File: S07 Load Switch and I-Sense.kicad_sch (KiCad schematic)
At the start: 62 parts, among them Q20 BSS138, Q21 BSS138, Q22 BSS138, U10 TLV9002IDSG, U6 TPS22811, U7 TPS22811, U8 TLV9002IDSG, U9 TPS22811

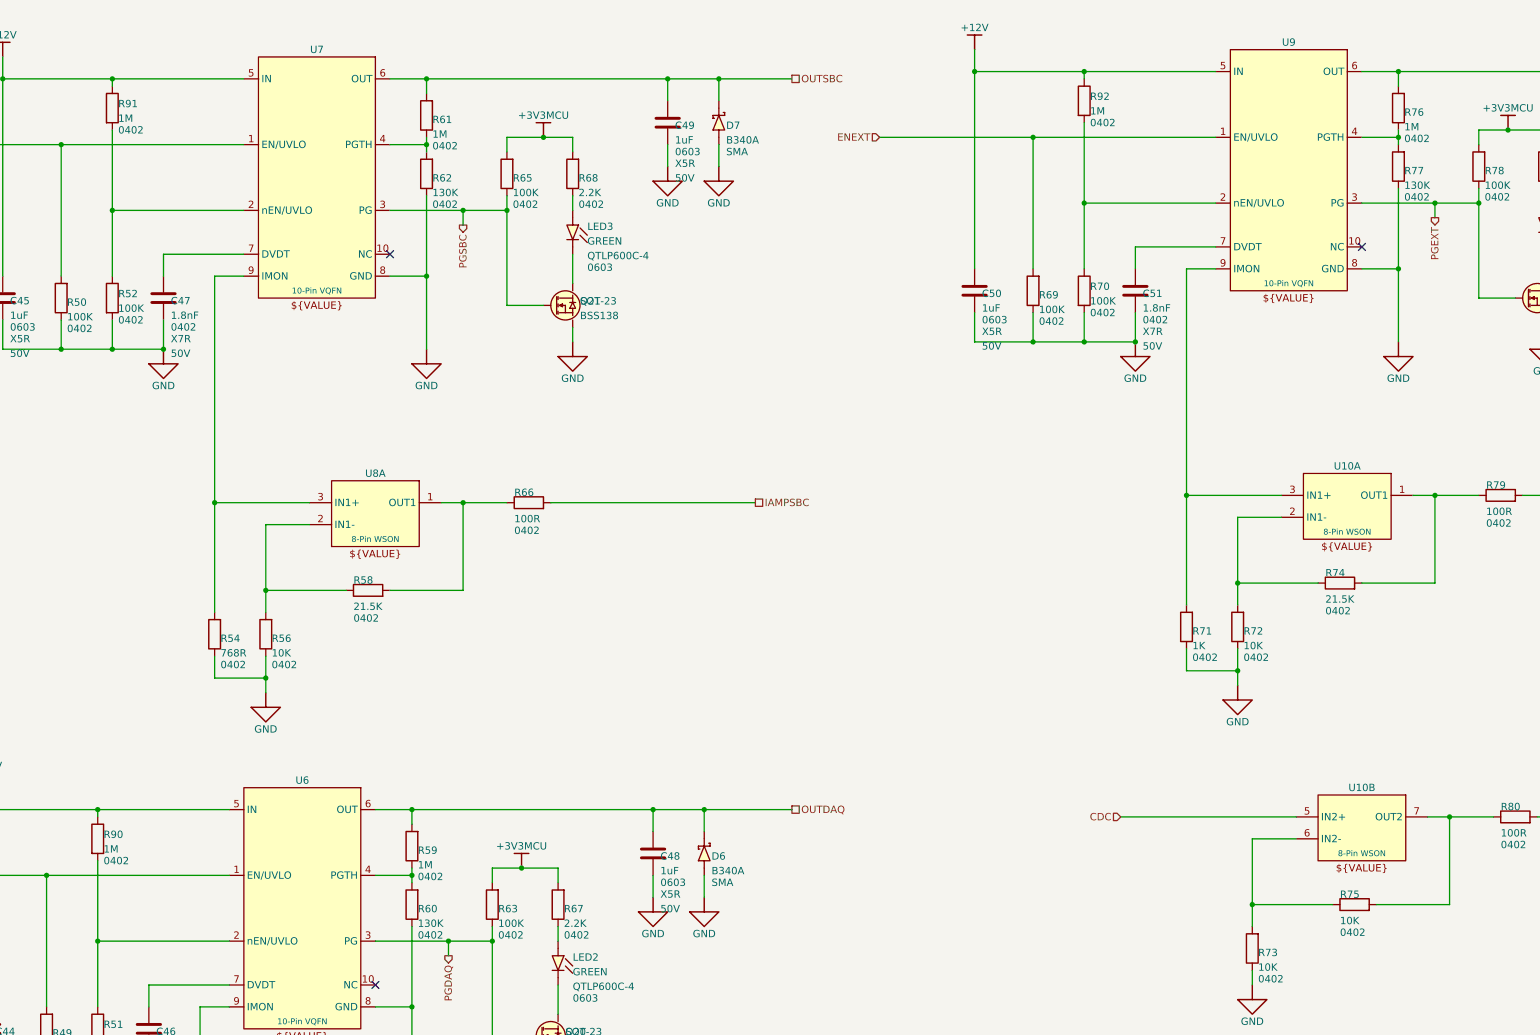
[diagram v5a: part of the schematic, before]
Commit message: Retune load-switch OVLO and PG dividers; add design constraint notes
- R90-R92 1M -> 1.07M: OVLO trips at 14.0 V (13.40-14.69 V) and recovers
  below 12.75 V (at least 12.23 V), so a tripped switch always comes back
  on the 12.03 V rail. R101 (Q23 gate divider) -> 1.07M to share the line.
- PGTH dividers R59/R61/R76 1M -> 100K and R60/R62/R77 130K -> 13K: same
  10.43 V threshold, but the +-1 uA pin leakage now moves it 0.1 V, not
  1 V; worst-case rising 10.93 V instead of 11.84 V.
- Schematic notes for the W16 constraints: J2 contacts (S01), R16 latching
  breaker and ED29/QE29 trip currents (S03), R19 vs L1 saturation (S04),
  R22 presence pull-up (S05), R42 and the U5 MODE/ILIMCOMP/VCC2 pins (S06),
  and the OVLO/PG divider settings (S07).
- README: OVLO and PG divider figures, and the EN_CONST_TDEAD default for
  the I2C build.

Co-Authored-By: Claude Opus 5.5 <noreply@anthropic.com>
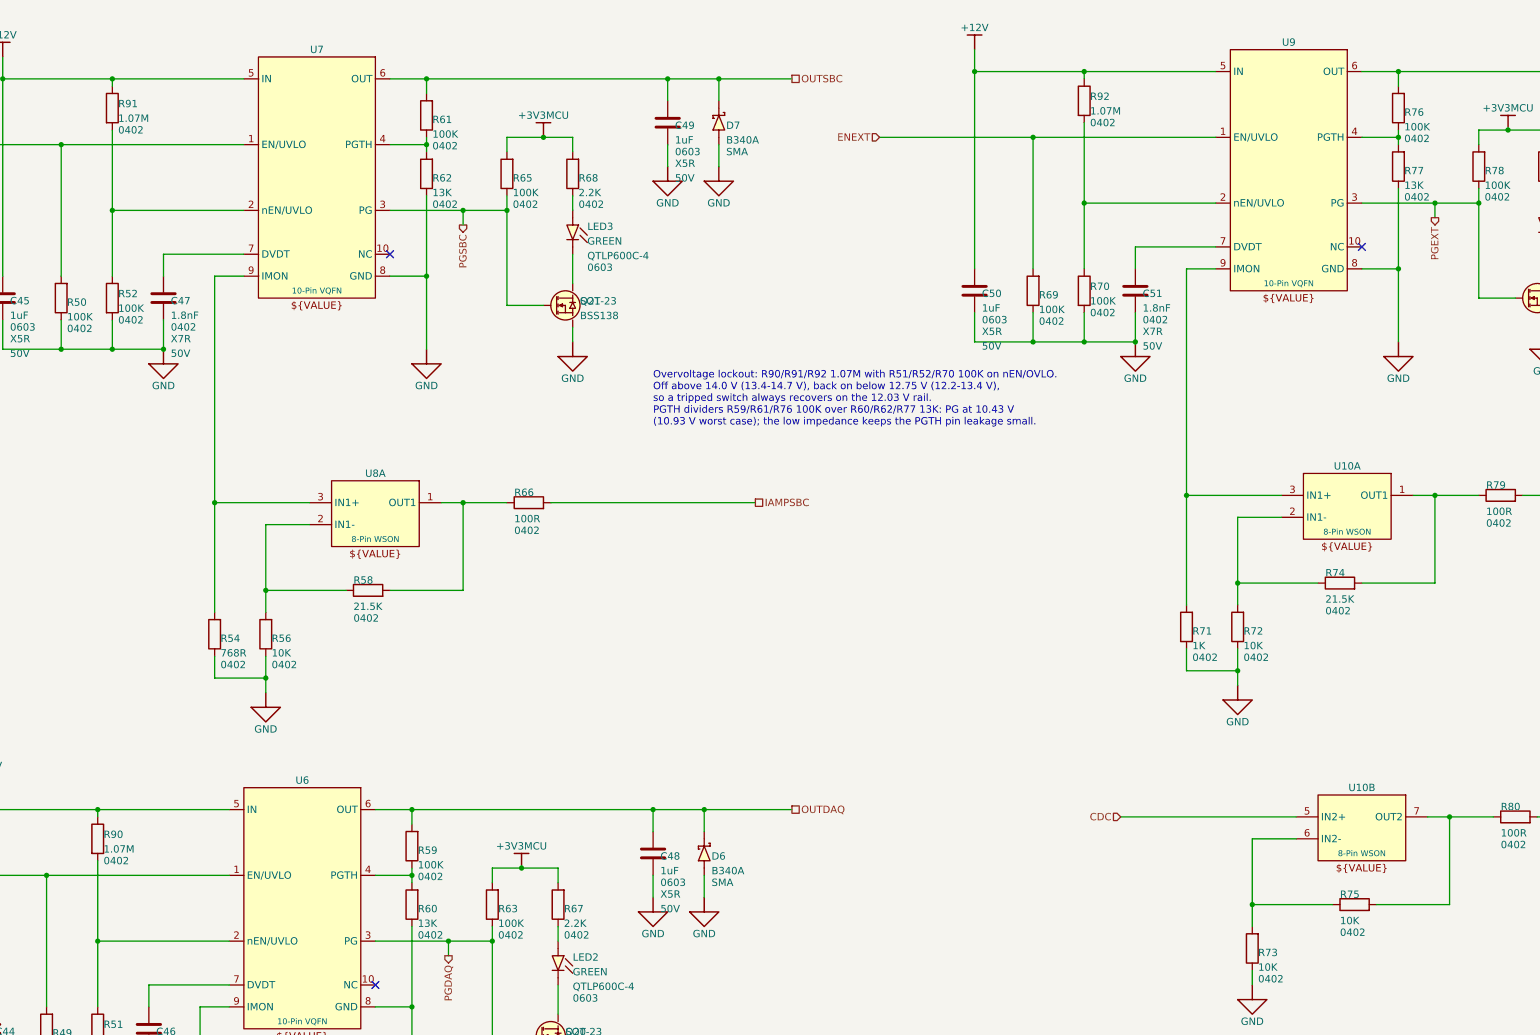
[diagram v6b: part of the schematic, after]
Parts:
- R59, R61, R76: value 1M -> 100K; ALTIUM_VALUE 1M -> 100K
- R60, R62, R77: value 130K -> 13K; ALTIUM_VALUE 130K -> 13K
- R90, R91, R92: value 1M -> 1.07M; ALTIUM_VALUE 1M -> 1.07M
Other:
- note added: "Overvoltage lockout: R90/R91/R92 1.07M with R51/R52/R70 100K on nEN/OVLO. Off above 14.0 V (13.4-14.7 V), back on below 12.75 V (12.2-13.4 V), so a tripped switch always recovers on the 12.03 V rail. PGTH dividers R59/R61/R76 100K over R60/R62/R77 13K: PG at 10.43 V (10.93 V worst case); the low impedance keeps the PGTH pin leakage small."
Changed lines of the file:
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@@
 	(generator_version "10.0")
 	(paper "A3")
+	(text "Overvoltage lockout: R90/R91/R92 1.07M with R51/R52/R70 100K on nEN/OVLO.\nOff above 14.0 V (13.4-14.7 V), back on below 12.75 V (12.2-13.4 V),\nso a tripped switch always recovers on the 12.03 V rail.\nPGTH dividers R59/R61/R76 100K over R60/R62/R77 13K: PG at 10.43 V\n(10.93 V worst case); the low impedance keeps the PGTH pin leakage small."
+		(exclude_from_sim no)
+		(at 170.18 97.79 0)
+		(effects
+			(font
+				(size 1.27 1.27)
+			)
+			(justify left top)
+		)
+	)
 	(text "5"
 		(exclude_from_sim no)
@@
 			)
 		)
-		(property "Value" "1M"
+		(property "Value" "1.07M"
 			(at 77.216 54.61 0)
 			(show_name no)
@@
 			)
 		)
-		(property "Description" "Resistor 1M 1% 0402"
+		(property "Description" "Resistor 1.07M 1% 0402"
 			(at 76.2 52.07 90)
 			(hide yes)
@@
 			)
 		)
-		(property "ALTIUM_VALUE" "1M"
+		(property "ALTIUM_VALUE" "1.07M"
 			(at 75.184 47.752 0)
 			(hide yes)
@@
 			)
 		)
-		(property "Value" "1M"
+		(property "Value" "100K"
 			(at 131.826 55.88 0)
 			(show_name no)
@@
 			)
 		)
-		(property "Description" "Resistor 1M 1% 0402"
+		(property "Description" "Resistor 100K 1% 0402"
 			(at 130.81 53.34 90)
 			(hide yes)
@@
 			)
 		)
-		(property "ALTIUM_VALUE" "1M"
+		(property "ALTIUM_VALUE" "100K"
 			(at 129.794 49.022 0)
 			(hide yes)
@@
 			)
 		)
-		(property "Value" "130K"
+		(property "Value" "13K"
 			(at 300.736 64.77 0)
 			(show_name no)
@@
 			)
 		)
-		(property "Description" "Resistor 130K 1% 0402"
+		(property "Description" "Resistor 13K 1% 0402"
 			(at 299.72 62.23 90)
 			(hide yes)
@@
 			)
 		)
-		(property "ALTIUM_VALUE" "130K"
+		(property "ALTIUM_VALUE" "13K"
 			(at 298.704 57.912 0)
 			(hide yes)
@@
 			)
 		)
-		(property "Value" "1M"
+		(property "Value" "1.07M"
 			(at 246.126 53.34 0)
 			(show_name no)
@@
 			)
 		)
-		(property "Description" "Resistor 1M 1% 0402"
+		(property "Description" "Resistor 1.07M 1% 0402"
 			(at 245.11 50.8 90)
 			(hide yes)
@@
 			)
 		)
-		(property "ALTIUM_VALUE" "1M"
+		(property "ALTIUM_VALUE" "1.07M"
 			(at 244.094 46.482 0)
 			(hide yes)
@@
 			)
 		)
-		(property "Value" "1M"
+		(property "Value" "100K"
 			(at 129.286 182.88 0)
 			(show_name no)
@@
 			)
 		)
-		(property "Description" "Resistor 1M 1% 0402"
+		(property "Description" "Resistor 100K 1% 0402"
 			(at 128.27 180.34 90)
 			(hide yes)
@@
 			)
 		)
-		(property "ALTIUM_VALUE" "1M"
+		(property "ALTIUM_VALUE" "100K"
 			(at 127.254 176.022 0)
 			(hide yes)
@@
 			)
 		)
-		(property "Value" "130K"
+		(property "Value" "13K"
 			(at 129.286 193.04 0)
 			(show_name no)
@@
 			)
 		)
-		(property "Description" "Resistor 130K 1% 0402"
+		(property "Description" "Resistor 13K 1% 0402"
 			(at 128.27 190.5 90)
 			(hide yes)
@@
 			)
 		)
-		(property "ALTIUM_VALUE" "130K"
+		(property "ALTIUM_VALUE" "13K"
 			(at 127.254 186.182 0)
 			(hide yes)
@@
 			)
 		)
-		(property "Value" "130K"
+		(property "Value" "13K"
 			(at 131.826 66.04 0)
 			(show_name no)
@@
 			)
 		)
-		(property "Description" "Resistor 130K 1% 0402"
+		(property "Description" "Resistor 13K 1% 0402"
 			(at 130.81 63.5 90)
 			(hide yes)
@@
 			)
 		)
-		(property "ALTIUM_VALUE" "130K"
+		(property "ALTIUM_VALUE" "13K"
 			(at 129.794 59.182 0)
 			(hide yes)
@@
 			)
 		)
-		(property "Value" "1M"
+		(property "Value" "100K"
 			(at 300.736 54.61 0)
 			(show_name no)
@@
 			)
 		)
-		(property "Description" "Resistor 1M 1% 0402"
+		(property "Description" "Resistor 100K 1% 0402"
 			(at 299.72 52.07 90)
 			(hide yes)
@@
 			)
 		)
-		(property "ALTIUM_VALUE" "1M"
+		(property "ALTIUM_VALUE" "100K"
 			(at 298.704 47.752 0)
 			(hide yes)
@@
 			)
 		)
-		(property "Value" "1M"
+		(property "Value" "1.07M"
 			(at 74.676 181.61 0)
 			(show_name no)
@@
 			)
 		)
-		(property "Description" "Resistor 1M 1% 0402"
+		(property "Description" "Resistor 1.07M 1% 0402"
 			(at 73.66 179.07 90)
 			(hide yes)
@@
 			)
 		)
-		(property "ALTIUM_VALUE" "1M"
+		(property "ALTIUM_VALUE" "1.07M"
 			(at 72.644 174.752 0)
 			(hide yes)

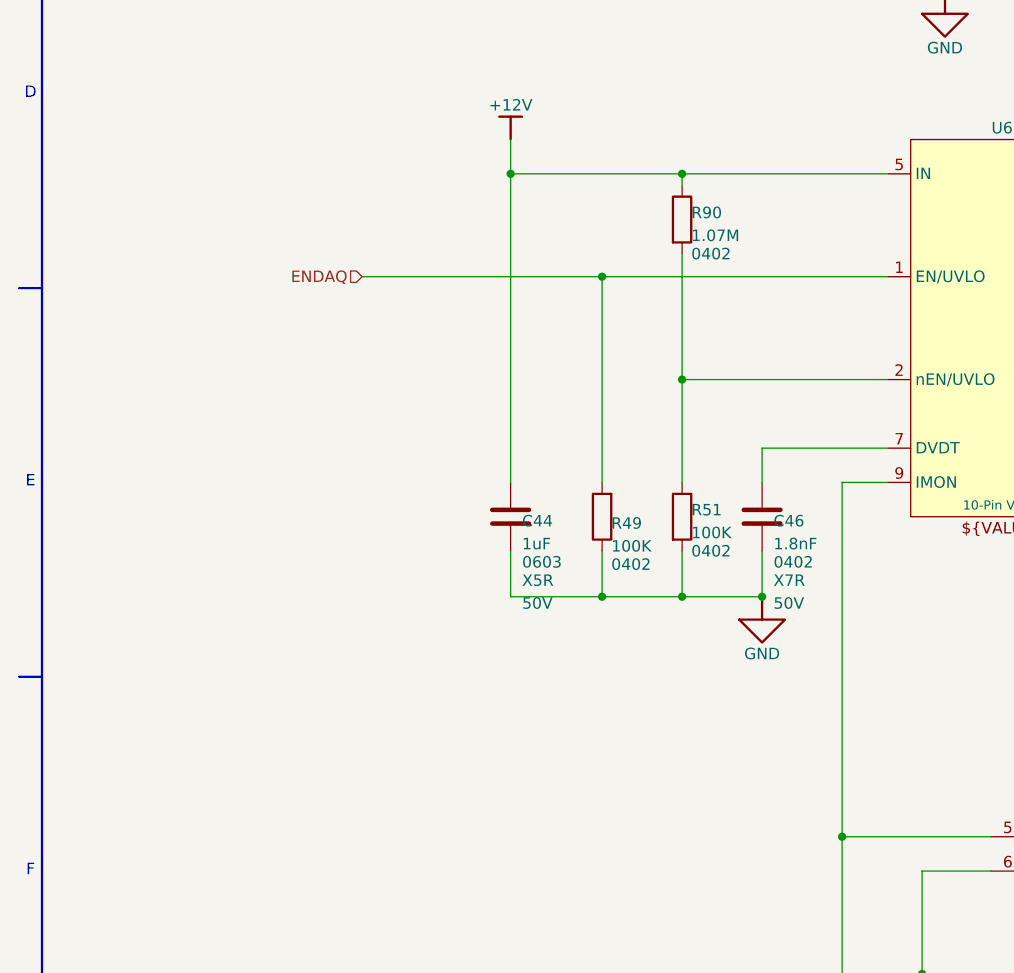
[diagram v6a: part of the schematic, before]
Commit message: Add an 11 V undervoltage lockout to the DAQ load switch
- R108 100K from +12V over R49 (100K -> 12K) on U6 EN/UVLO: on at 11.2 V
  (10.77-11.69 V), off at 10.17 V (9.83-10.66 V). The TPS22811's fixed
  hysteresis makes 11 V the turn-on point.
- Q24 (BSS138) from EN/UVLO to GND takes over the enable. Its gate is biased
  from +12V by R109 100K / R110 27K (2.55 V), so U6 stays in shutdown when
  the expander is in reset, unpowered, or the MCU board is off.
- The expander net ENDAQ is now nENDAQ, active low (S07, S08, root sheet).
  The gate stays under 3.3 V, so P0_0 can stay push-pull and the R97
  fallback can drive it from a 3.3 V MCU pin.
- S07 note marks the DAQ circuit as deliberate; S08 notes and README
  updated.

The PCB still needs Update PCB from Schematic: Q24 and R108-R110 are
missing, R49 has its old value, and /ENDAQ is split into two nets.

Co-Authored-By: Claude Opus 5.5 <noreply@anthropic.com>
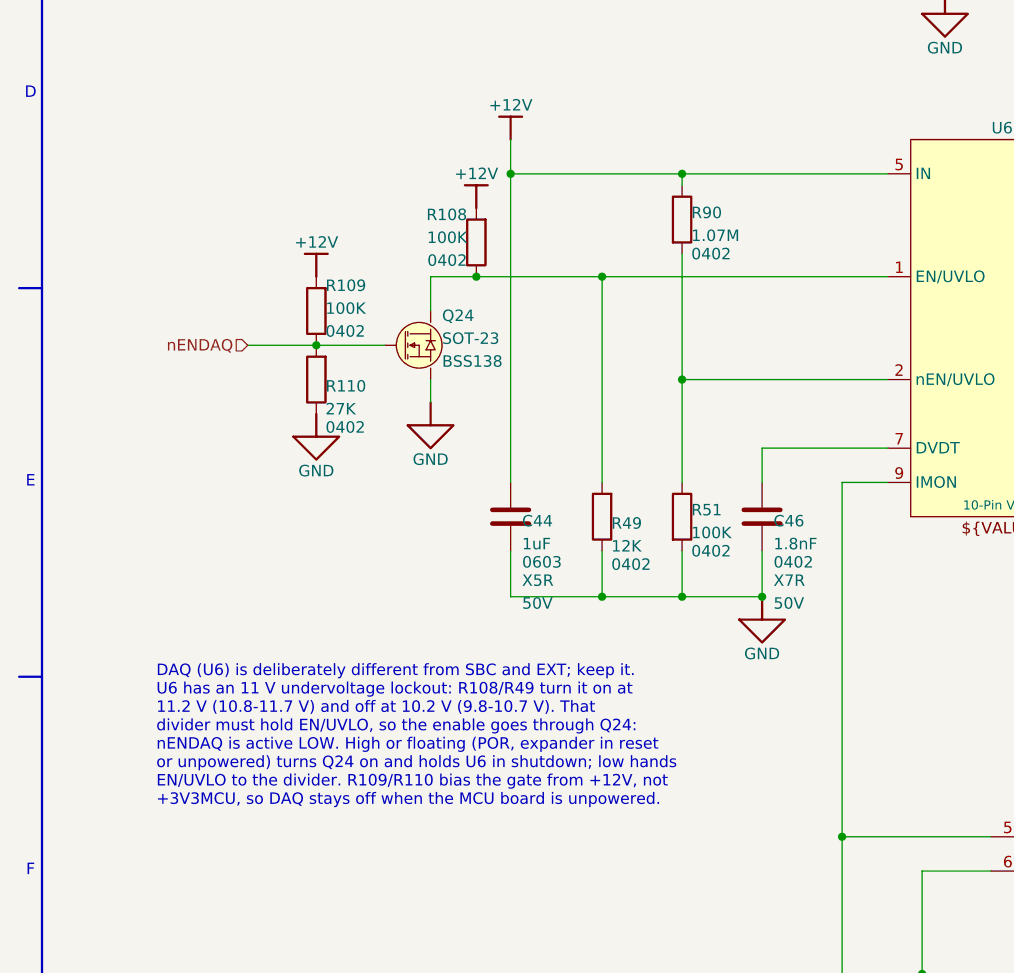
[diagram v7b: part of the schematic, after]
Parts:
- added Q24: BSS138, Package_TO_SOT_SMD:SOT-23, symbol Lattech Systems:Transistor N-Channel MOSFET 50V BSS138 SOT-23
- added R108, R109: 100K, Resistor_SMD:R_0402_1005Metric, symbol Device:R
- added R110: 27K, Resistor_SMD:R_0402_1005Metric, symbol Device:R
- R49: value 100K -> 12K; ALTIUM_VALUE 100K -> 12K
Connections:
- net +12V: now also R108.2, R109.2
- net GND: now also Q24.2 (S), R110.1
- net ENDAQ: no longer names the net of R49.2, U6.1 (EN/UVLO)
- net ENDAQ: now also Q24.3 (D), R108.1
- new net nENDAQ: Q24.1 (G), R109.1, R110.2
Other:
- note added: "DAQ (U6) is deliberately different from SBC and EXT; keep it. U6 has an 11 V undervoltage lockout: R108/R49 turn it on at 11.2 V (10.8-11.7 V) and off at 10.2 V (9.8-10.7 V). That divider must hold EN/UVLO, so the enable goes through Q24: nENDAQ is active LOW. High or floating (POR, expander in reset or unpowered) turns Q24 on and holds U6 in shutdown; low hands EN/UVLO to the divider. R109/R110 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"
